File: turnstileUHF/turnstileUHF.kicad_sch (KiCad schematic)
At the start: 37 parts, among them Q1 PMOS, SW1 SW_DIP_x01

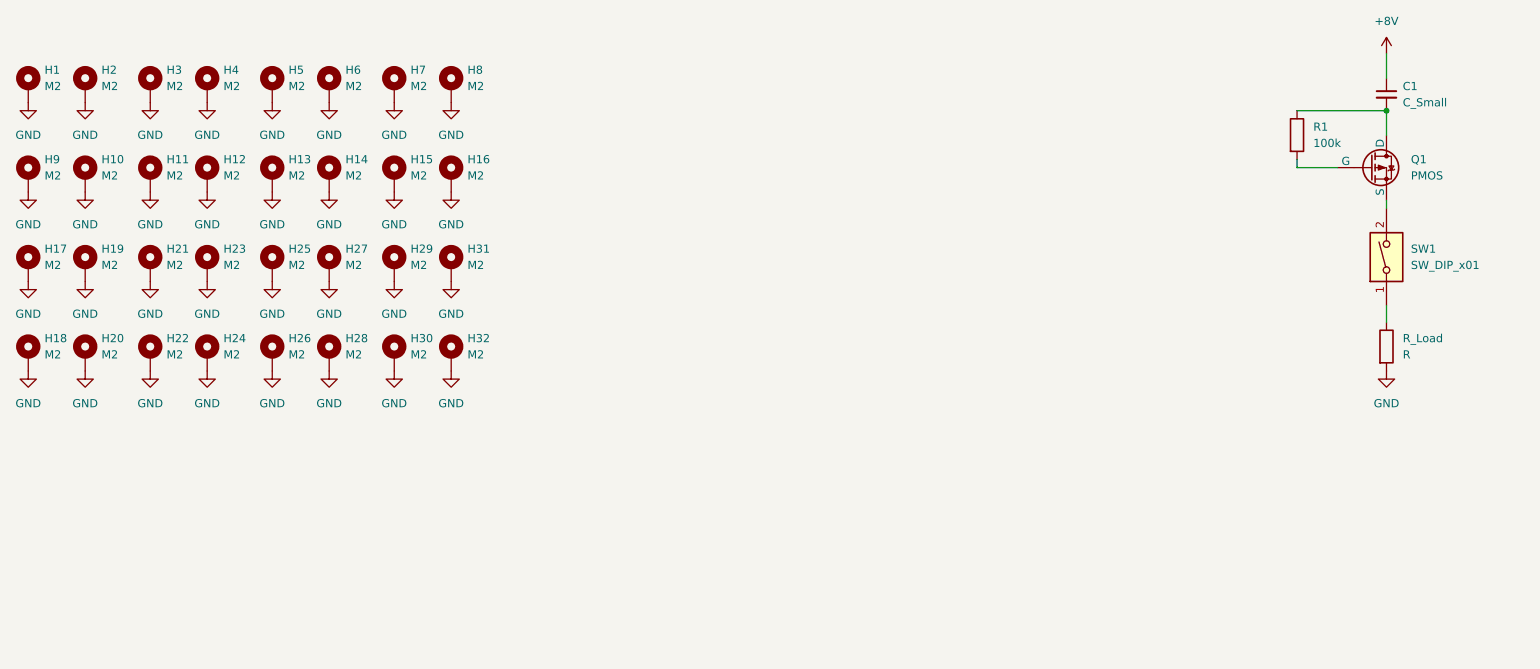
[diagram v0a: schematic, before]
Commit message: burn wire routing
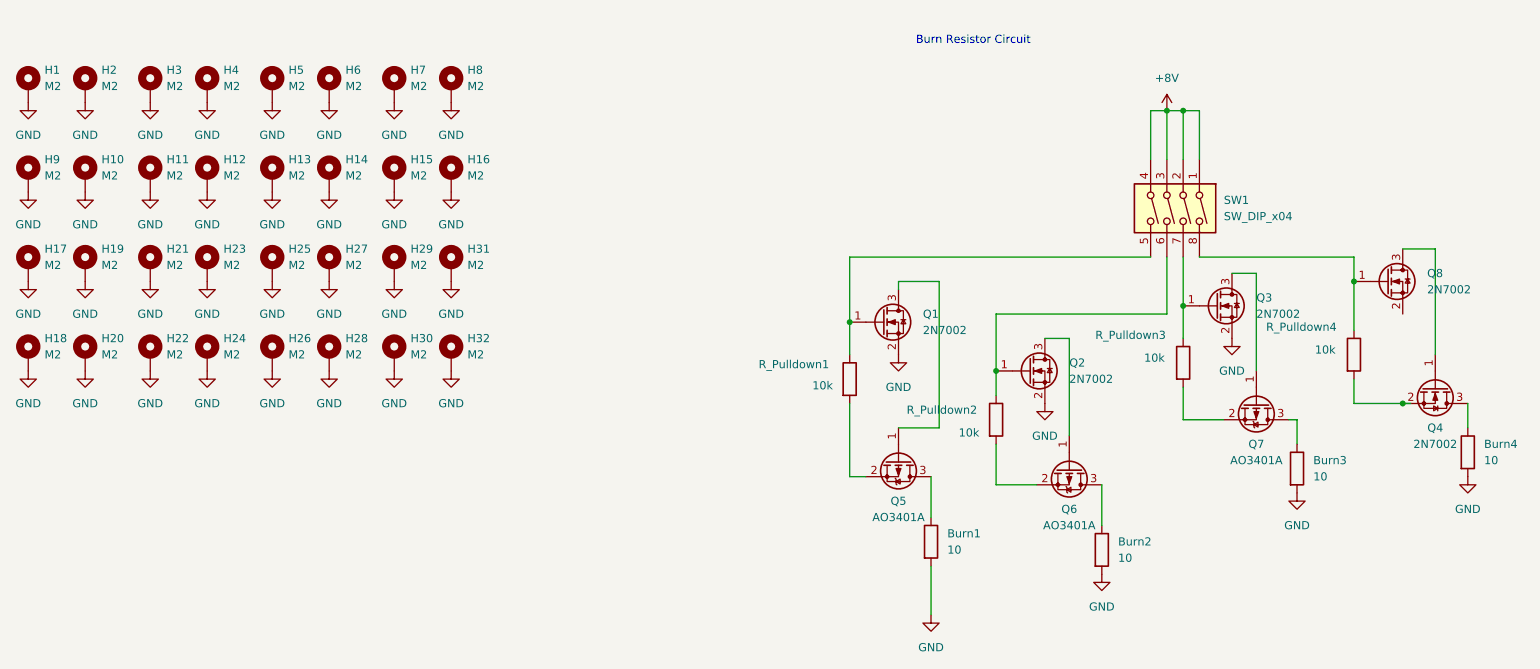
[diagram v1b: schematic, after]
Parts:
- removed C1: C_Small, symbol Device:C_Small
- removed Q1: PMOS, symbol Simulation_SPICE:PMOS
- removed R1: 100k, symbol Device:R
- removed R_Load: R, symbol Device:R
- removed SW1: SW_DIP_x01, symbol Switch:SW_DIP_x01
- added Burn1, Burn2, Burn3, Burn4: 10, Resistor_SMD:R_2512_6332Metric_Pad1.40x3.35mm_HandSolder, symbol Device:R
- added Q1, Q2, Q3, Q4, Q8: 2N7002, Package_TO_SOT_SMD:SOT-23, symbol Transistor_FET:2N7002
- added Q5, Q6, Q7: AO3401A, Package_TO_SOT_SMD:SOT-23, symbol Transistor_FET:AO3401A
- added R_Pulldown1, R_Pulldown2, R_Pulldown3, R_Pulldown4: 10k, Resistor_SMD:R_01005_0402Metric_Pad0.57x0.30mm_HandSolder, symbol Device:R
- added SW1: SW_DIP_x04, symbol Switch:SW_DIP_x04
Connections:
- net +8V: now also SW1.1, SW1.2, SW1.3, SW1.4
- net GND: now also Burn1.2, Burn2.2, Burn3.2, Burn4.2, Q1.2 (S), Q2.2 (S), Q3.2 (S)
- new net: Burn3.1, Q7.3 (D)
- new net: Q1.3 (D), Q5.1 (G)
- new net: Q5.2 (S), R_Pulldown1.2
- new net: Burn1.1, Q5.3 (D)
- new net: Burn2.1, Q6.3 (D)
- new net: Q1.1 (G), R_Pulldown1.1, SW1.5
- new net: Q3.1 (G), R_Pulldown3.1, SW1.7
- new net: Q7.2 (S), R_Pulldown3.2
- new net: Q2.1 (G), R_Pulldown2.1, SW1.6
- new net: Q2.3 (D), Q6.1 (G)
- new net: Q6.2 (S), R_Pulldown2.2
- new net: Q4.1 (G), Q8.3 (D)
- new net: Q4.2 (S), R_Pulldown4.2
- new net: Burn4.1, Q4.3 (D)
- new net: Q8.1 (G), R_Pulldown4.1, SW1.8
- new net: Q3.3 (D), Q7.1 (G)
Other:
- note added: "Burn Resistor Circuit"
